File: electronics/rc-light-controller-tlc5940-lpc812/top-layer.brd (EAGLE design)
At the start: 26.7 x 18 mm, 0 parts

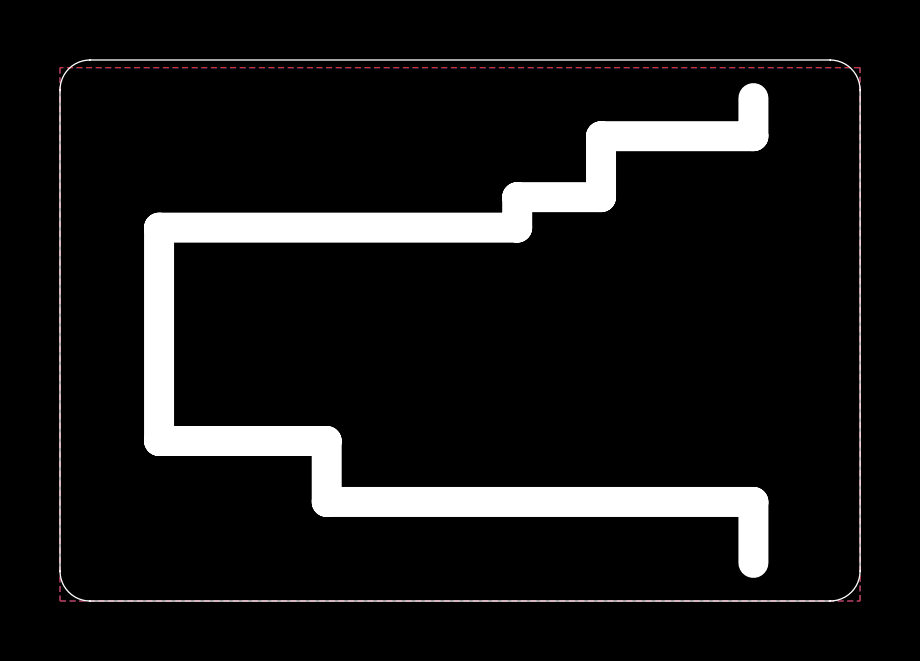
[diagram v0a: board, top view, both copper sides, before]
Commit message: Swap SCLK and XLAT for better layout
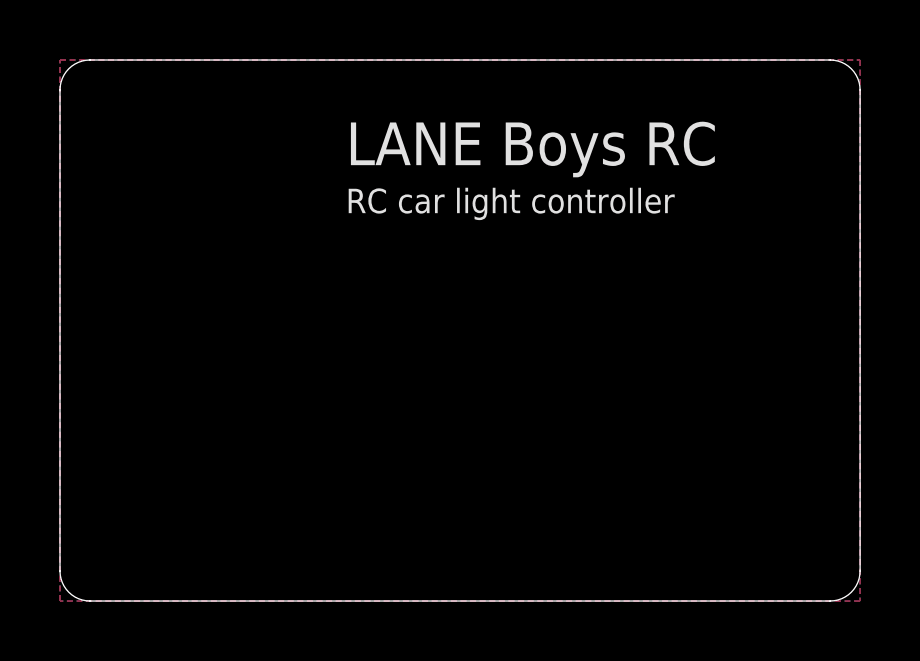
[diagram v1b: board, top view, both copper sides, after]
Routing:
- added copper zone on layer 1, net S$1
- added copper zone on layer 16, net S$1
- removed copper zone on layer 1, net GND
- removed copper zone on layer 16, net N$1
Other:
- outline, holes or cut-outs redrawn
- board text added: "CH3"
- board text added: "GND"
- board text added: "LANE Boys RC"
- board text added: "OUT/ISP"
- board text added: "RC car light controller"
- board text added: "Rev 1"
- board text added: "ST/Rx"
- board text added: "TH/Tx"
- board text added: "TLC5940 + LPC812"
- board text added: "Vdd"
- board text added: "http://goo.gl/Vif9VM"
